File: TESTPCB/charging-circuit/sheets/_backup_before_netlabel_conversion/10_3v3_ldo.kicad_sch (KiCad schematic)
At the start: 9 parts, among them P7 1.27mm/1*3p, U6 MT3608

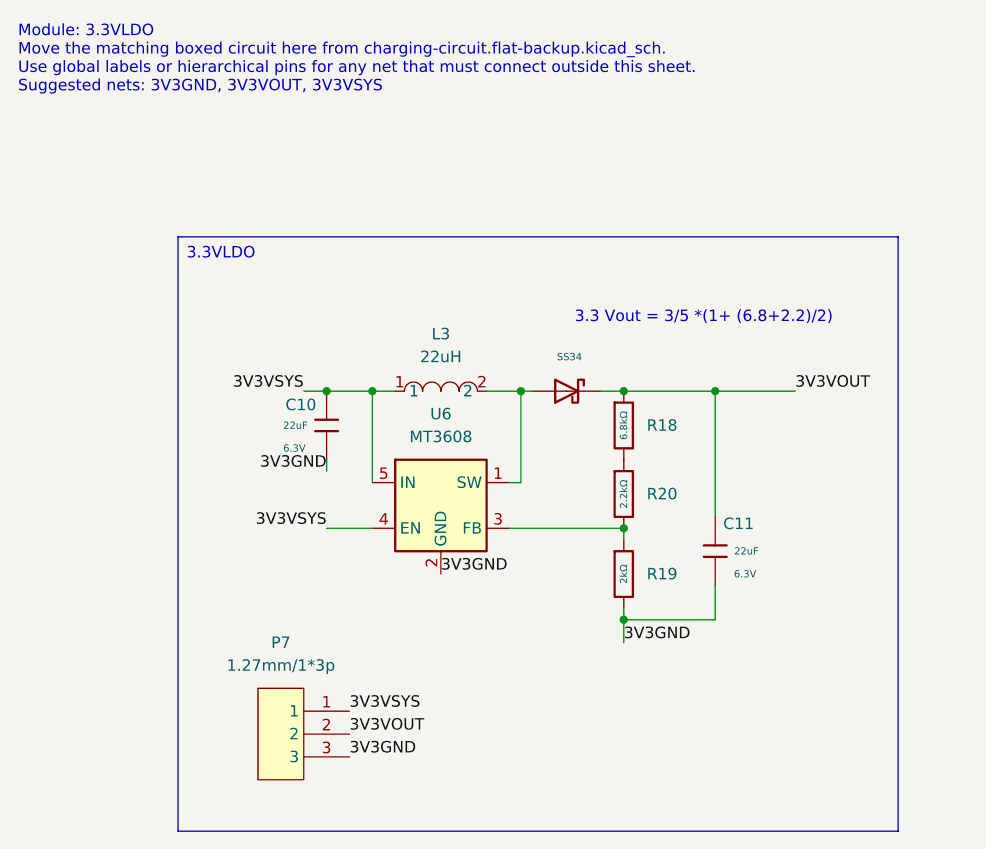
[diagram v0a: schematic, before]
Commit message: Fixed formatting issues, now the hierachal sheets are all labeled as net labels and when we want to expose their pins we will make them into hierchal or global pins
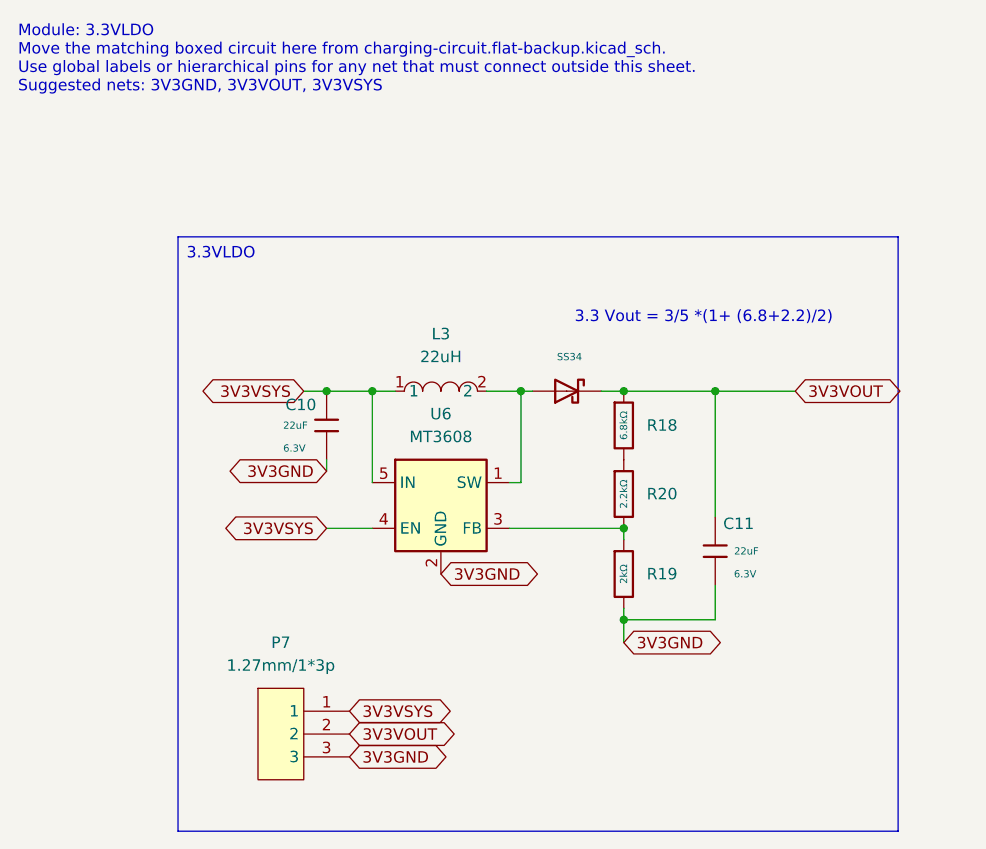
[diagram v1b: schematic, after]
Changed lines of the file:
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@@
 		)
 	)
-	(label "3V3VSYS"
+	(global_label "3V3VSYS"
+		(shape bidirectional)
 		(at 57.15 62.23 180)
 		(effects
@@
 			(justify right bottom)
 		)
+		(property "Intersheetrefs" "${INTERSHEET_REFS}"
+			(at 57.15 62.23 0)
+			(effects
+				(font
+					(size 1.27 1.27)
+				)
+				(hide yes)
+			)
+		)
 	)
-	(label "3V3GND"
+	(global_label "3V3GND"
+		(shape bidirectional)
 		(at 72.39 82.55 0)
 		(effects
@@
 			(justify left bottom)
 		)
+		(property "Intersheetrefs" "${INTERSHEET_REFS}"
+			(at 72.39 82.55 0)
+			(effects
+				(font
+					(size 1.27 1.27)
+				)
+				(hide yes)
+			)
+		)
 	)
-	(label "3V3VSYS"
+	(global_label "3V3VSYS"
+		(shape bidirectional)
 		(at 59.69 77.47 180)
 		(effects
@@
 			(justify right bottom)
 		)
+		(property "Intersheetrefs" "${INTERSHEET_REFS}"
+			(at 59.69 77.47 0)
+			(effects
+				(font
+					(size 1.27 1.27)
+				)
+				(hide yes)
+			)
+		)
 	)
-	(label "3V3VSYS"
+	(global_label "3V3VSYS"
+		(shape bidirectional)
 		(at 62.23 97.79 0)
 		(effects
@@
 			(justify left bottom)
 		)
+		(property "Intersheetrefs" "${INTERSHEET_REFS}"
+			(at 62.23 97.79 0)
+			(effects
+				(font
+					(size 1.27 1.27)
+				)
+				(hide yes)
+			)
+		)
 	)
-	(label "3V3GND"
+	(global_label "3V3GND"
+		(shape bidirectional)
 		(at 62.23 102.87 0)
 		(effects
@@
 			(justify left bottom)
 		)
+		(property "Intersheetrefs" "${INTERSHEET_REFS}"
+			(at 62.23 102.87 0)
+			(effects
+				(font
+					(size 1.27 1.27)
+				)
+				(hide yes)
+			)
+		)
 	)
-	(label "3V3VOUT"
+	(global_label "3V3VOUT"
+		(shape bidirectional)
 		(at 111.76 62.23 0)
 		(effects
@@
 			(justify left bottom)
 		)
+		(property "Intersheetrefs" "${INTERSHEET_REFS}"
+			(at 111.76 62.23 0)
+			(effects
+				(font
+					(size 1.27 1.27)
+				)
+				(hide yes)
+			)
+		)
 	)
-	(label "3V3GND"
+	(global_label "3V3GND"
+		(shape bidirectional)
 		(at 92.71 90.17 0)
 		(effects
@@
 			(justify left bottom)
 		)
+		(property "Intersheetrefs" "${INTERSHEET_REFS}"
+			(at 92.71 90.17 0)
+			(effects
+				(font
+					(size 1.27 1.27)
+				)
+				(hide yes)
+			)
+		)
 	)
-	(label "3V3GND"
+	(global_label "3V3GND"
+		(shape bidirectional)
 		(at 59.69 71.12 180)
 		(effects
@@
 			(justify right bottom)
 		)
+		(property "Intersheetrefs" "${INTERSHEET_REFS}"
+			(at 59.69 71.12 0)
+			(effects
+				(font
+					(size 1.27 1.27)
+				)
+				(hide yes)
+			)
+		)
 	)
-	(label "3V3VOUT"
+	(global_label "3V3VOUT"
+		(shape bidirectional)
 		(at 62.23 100.33 0)
 		(effects
@@
 			(justify left bottom)
 		)
+		(property "Intersheetrefs" "${INTERSHEET_REFS}"
+			(at 62.23 100.33 0)
+			(effects
+				(font
+					(size 1.27 1.27)
+				)
+				(hide yes)
+			)
+		)
 	)
